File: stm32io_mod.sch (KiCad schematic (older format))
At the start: 44 parts, among them J1 UART, M1 BluePill, Q1 BC858, Q2 BC858, Q3 BC858, Q4 BC858, SW1 button_1, SW2 button_2, SW3 button_3, SW4 button_4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

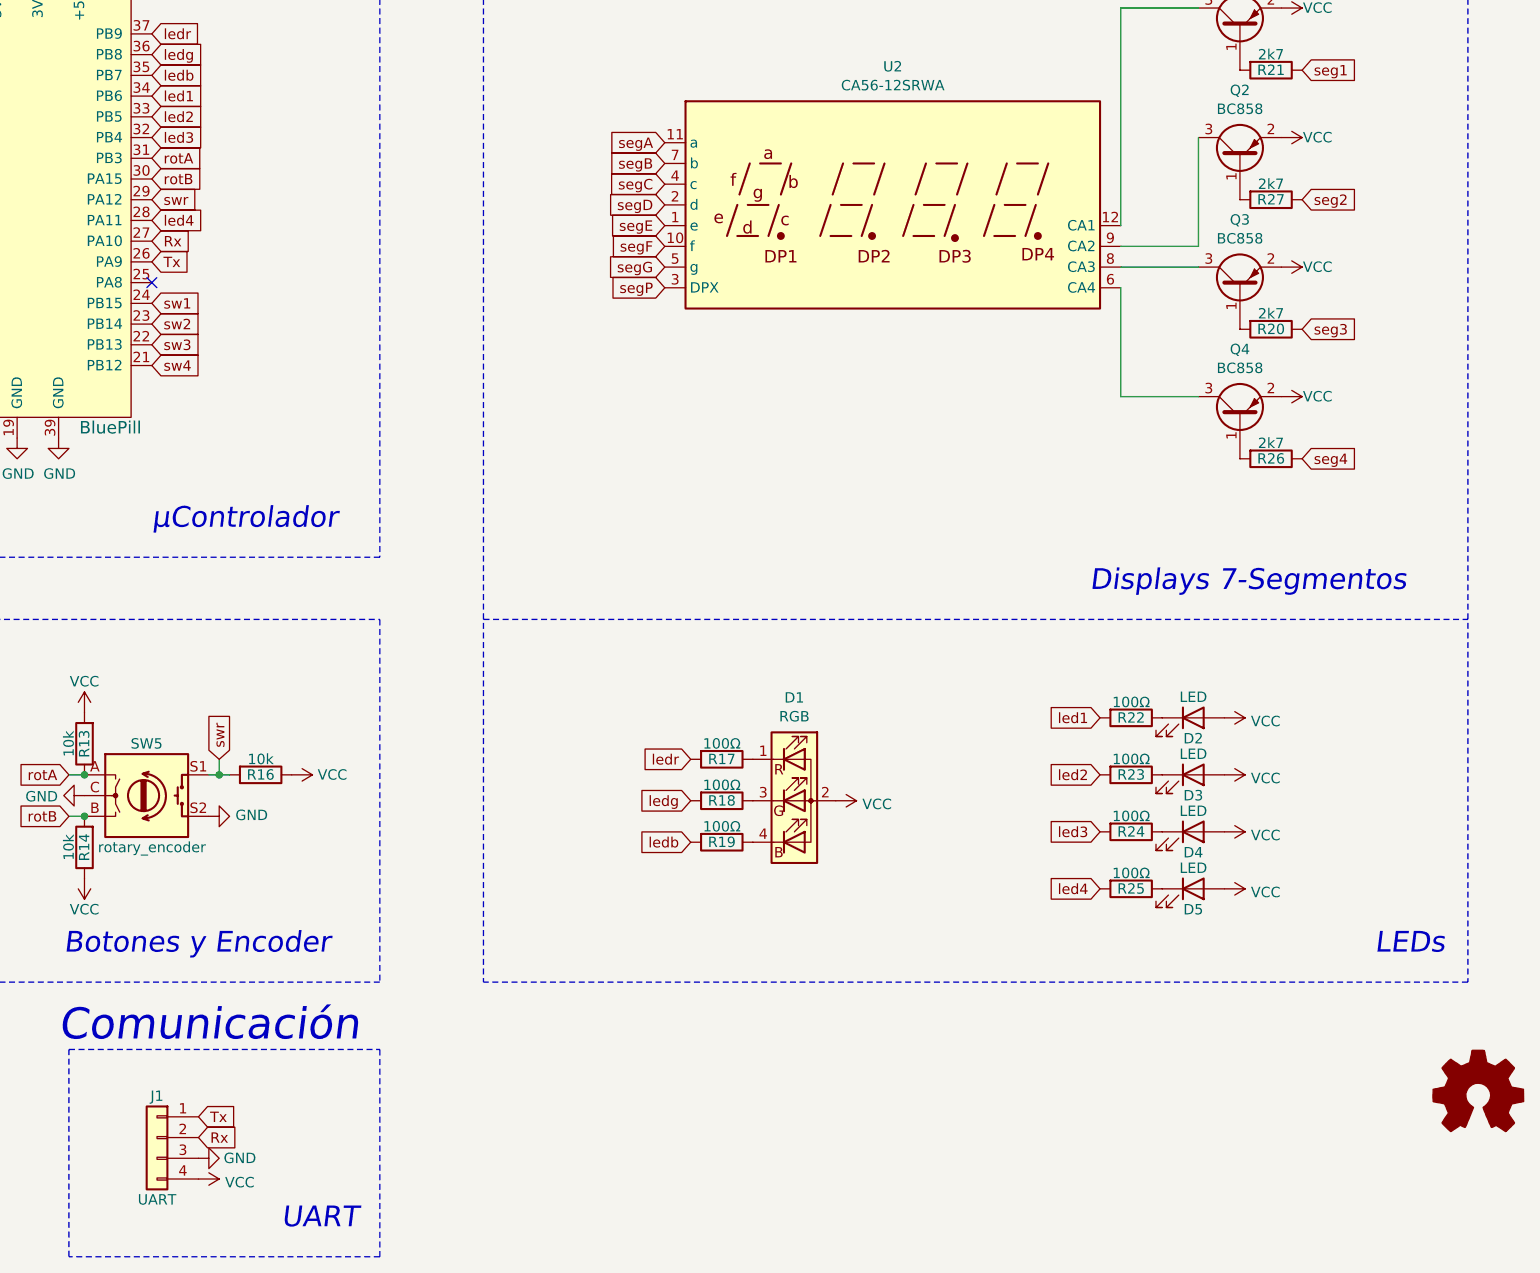
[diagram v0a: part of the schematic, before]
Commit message: Se mejoró el plano de masa
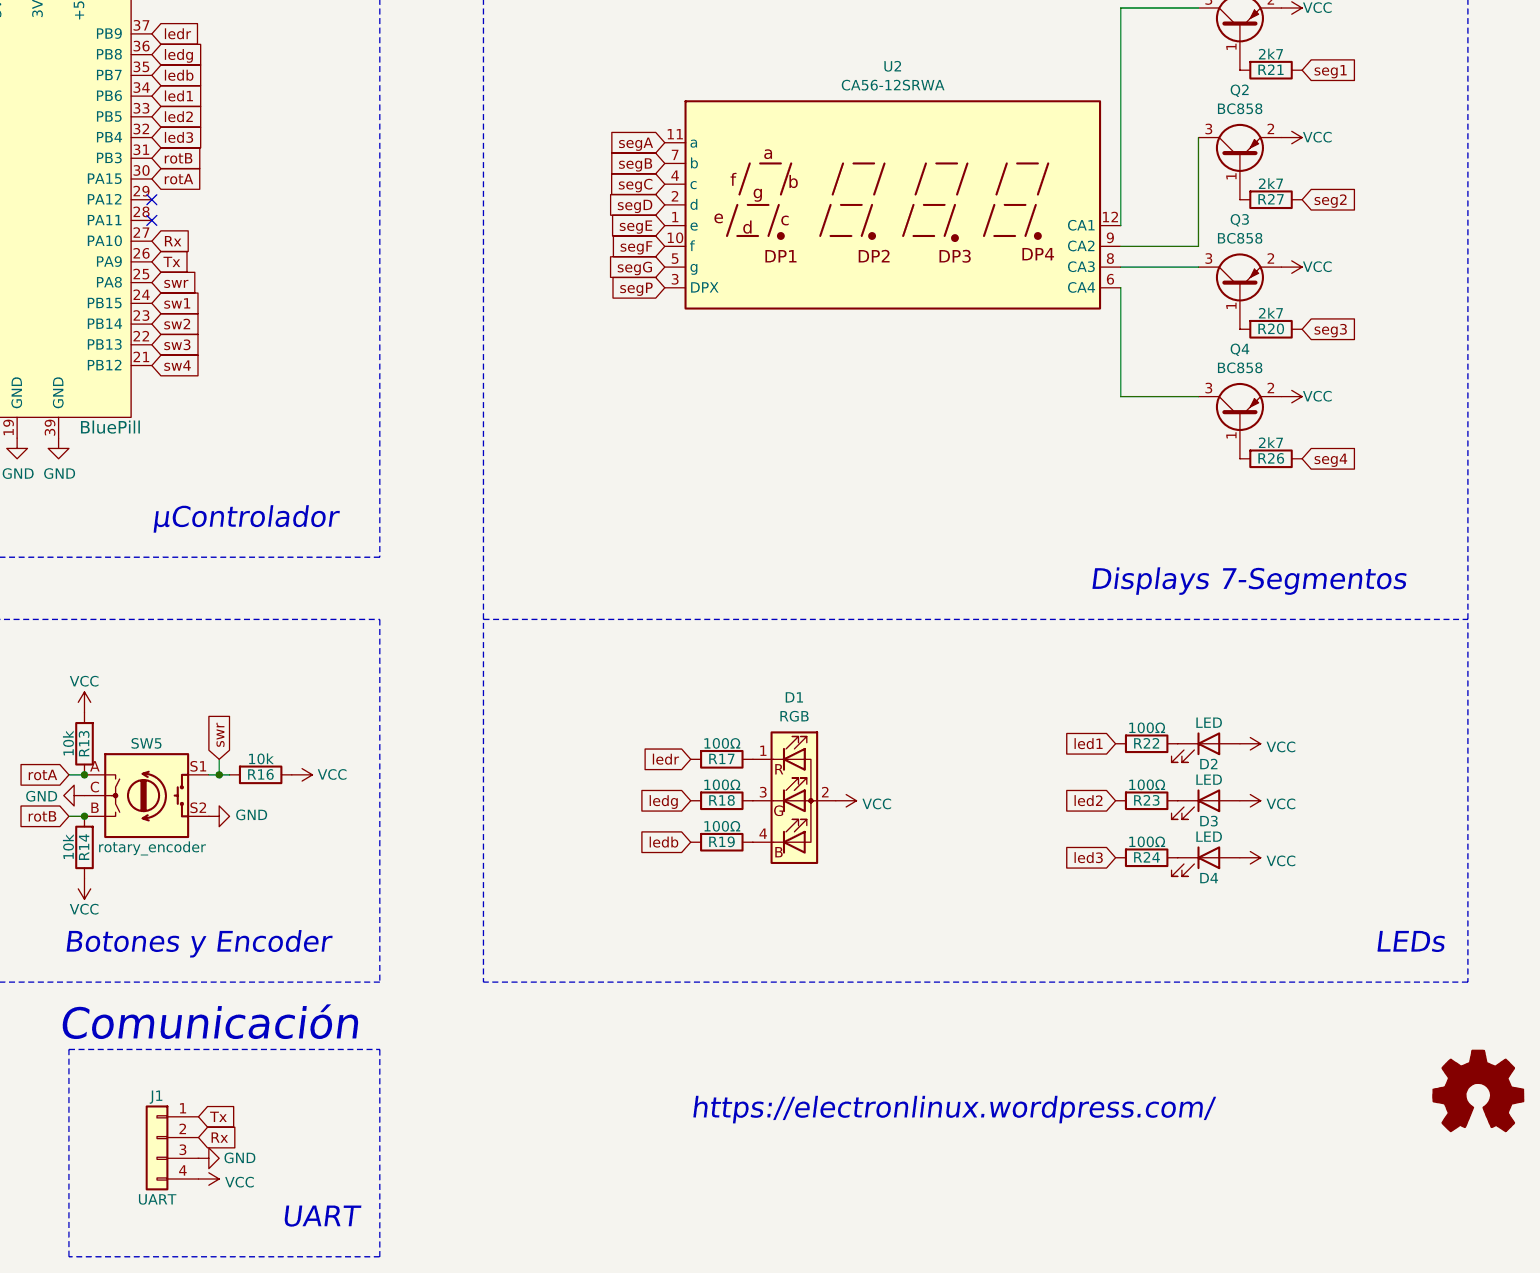
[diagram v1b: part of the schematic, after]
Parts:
- removed D5: LED, LED_THT:LED_D3.0mm_Clear, symbol Device:LED
- removed R25: 100Ω, Resistor_SMD:R_0805_2012Metric_Pad1.15x1.40mm_HandSolder, symbol Device:R
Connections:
- net rotA: now also M1.30 (PA15); no longer M1.31 (PB3)
- net rotB: now also M1.31 (PB3); no longer M1.30 (PA15)
- net swr: now also M1.25 (PA8); no longer M1.29 (PA12)
- net led4: no longer names the net of M1.28 (PA11)
- no-connect marks 7 -> 8
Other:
- note added: "https://electronlinux.wordpress.com/"
- moved on the sheet: D2, D3, D4, R22, R23, R24
